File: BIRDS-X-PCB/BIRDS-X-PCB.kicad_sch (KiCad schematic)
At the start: 18 parts, among them J101 LPC-50M2LG

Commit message: Major layout
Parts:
- removed H105, H106, H107, H108, H109, H110, H111, H112, H113, H114, H115, H116: MountingHole, BIRDS-X_Footprints_Lib:MountingHole_2mm, symbol Mechanical:MountingHole
- removed TP101: TestPoint, TestPoint:TestPoint_Pad_D1.5mm, symbol Connector:TestPoint
- added J102, J103, J104: RFShield_OnePiece, RF_Shielding:Laird_Technologies_97-2003_12.70x13.37mm, symbol Device:RFShield_OnePiece
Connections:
- net GND: now also J102.1 (Shield), J103.1 (Shield), J104.1 (Shield)
- no-connect marks 40 -> 41
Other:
- added sheet TempSensors (TempSensors.kicad_sch)
- sheet RadfetExperiment ports: added none; removed I2C_SCL, I2C_SDA
- note removed: "Radiation Shielding Mounting"

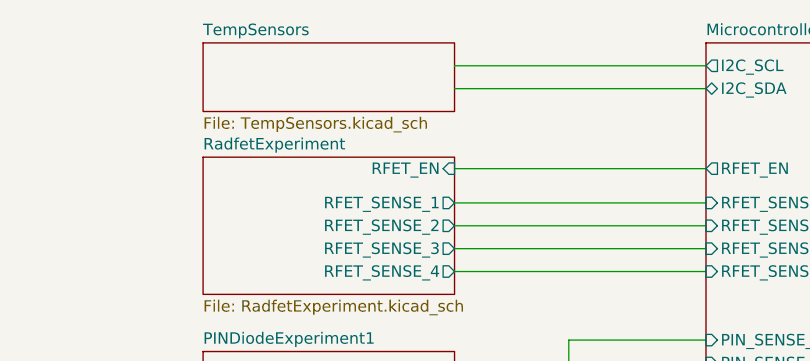
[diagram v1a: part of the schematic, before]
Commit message: Do most of routing
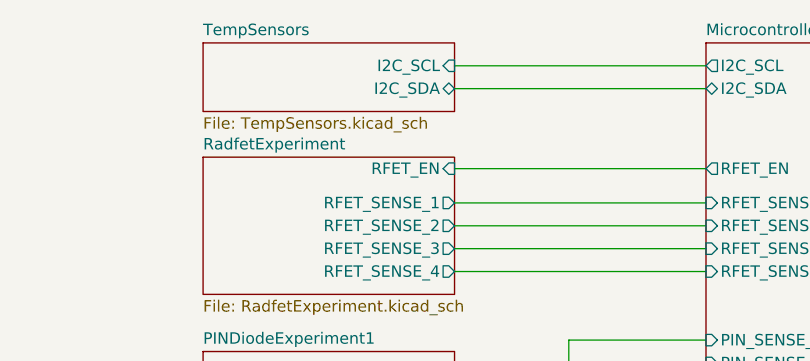
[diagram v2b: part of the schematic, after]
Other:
- sheet TempSensors ports: added I2C_SCL, I2C_SDA; removed none
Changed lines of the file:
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@@
       (effects (font (size 1.27 1.27)) (justify left top))
+    )
+    (pin "I2C_SCL" input (at 118.11 20.32 0)
+      (effects (font (size 1.27 1.27)) (justify right))
+    )
+    (pin "I2C_SDA" bidirectional (at 118.11 22.86 0)
+      (effects (font (size 1.27 1.27)) (justify right))
     )
     (instances

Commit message: Fix all DRC
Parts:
- J102, J103, J104: footprint RF_Shielding:Laird_Technologies_97-2003_12.70x13.37mm -> RF_Shielding:Laird_Technologies_BMI-S-101_13.66x12.70mm
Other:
- note added: "RF Shield Footprint: 12.70x13.66mm = 0.5 x 0.538""
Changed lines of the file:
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@@
     (stroke (width 0) (type default))
+  )
+  (text "RF Shield Footprint:\n12.70x13.66mm = 0.5 x 0.538\"" (at 58.42 134.62 0)
+    (effects (font (size 1.27 1.27)) (justify left bottom))
   )
   (text "Use SUP_3V3_2 as main power, per ICD" (at 195.58 118.11 0)
@@
       (effects (font (size 1.27 1.27)) (justify left))
     )
-    (property "Footprint" "RF_Shielding:Laird_Technologies_97-2003_12.70x13.37mm" (at 35.56 99.06 0)
+    (property "Footprint" "RF_Shielding:Laird_Technologies_BMI-S-101_13.66x12.70mm" (at 35.56 99.06 0)
       (effects (font (size 1.27 1.27)) hide)
     )
@@
       (effects (font (size 1.27 1.27)) (justify left))
     )
-    (property "Footprint" "RF_Shielding:Laird_Technologies_97-2003_12.70x13.37mm" (at 35.56 149.86 0)
+    (property "Footprint" "RF_Shielding:Laird_Technologies_BMI-S-101_13.66x12.70mm" (at 35.56 149.86 0)
       (effects (font (size 1.27 1.27)) hide)
     )
@@
       (effects (font (size 1.27 1.27)) (justify left))
     )
-    (property "Footprint" "RF_Shielding:Laird_Technologies_97-2003_12.70x13.37mm" (at 35.56 124.46 0)
-      (effects (font (size 1.27 1.27)) hide)
-    )
+    (property "Footprint" "RF_Shielding:Laird_Technologies_BMI-S-101_13.66x12.70mm" (at 35.56 124.46 0)
+      (effects (font (size 1.27 1.27)) hide)
+    )

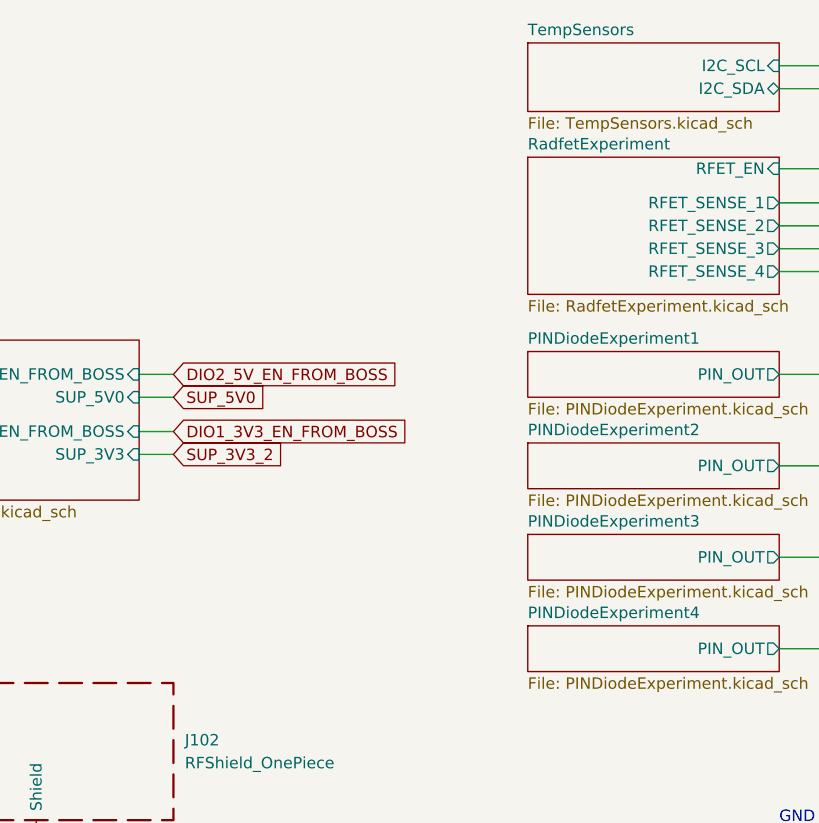
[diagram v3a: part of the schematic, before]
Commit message: Refactor jumper for PIN experiment power
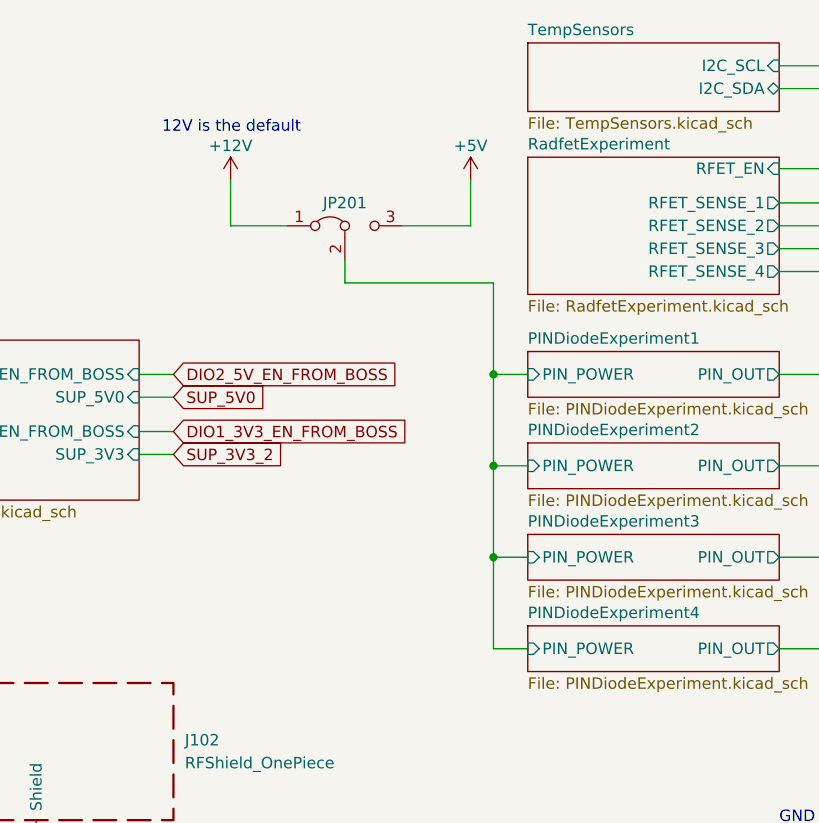
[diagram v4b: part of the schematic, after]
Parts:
- added JP201: Jumper_3_Bridged12, Jumper:SolderJumper-3_P1.3mm_Open_RoundedPad1.0x1.5mm_NumberLabels, symbol Jumper:Jumper_3_Bridged12
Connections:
- new net +12V: JP201.1 (A)
- new net +5V: JP201.3 (B)
- new net PINDiodeExperiment1/PIN_POWER: JP201.2 (C)
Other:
- sheet PINDiodeExperiment1 ports: added PIN_POWER; removed none
- sheet PINDiodeExperiment2 ports: added PIN_POWER; removed none
- sheet PINDiodeExperiment3 ports: added PIN_POWER; removed none
- sheet PINDiodeExperiment4 ports: added PIN_POWER; removed none
- note added: "12V is the default"
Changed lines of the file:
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@@
   (junction (at 181.61 102.87) (diameter 0) (color 0 0 0 0)
+  )
+  (junction (at 86.36 64.77) (diameter 0) (color 0 0 0 0)
+  )
+  (junction (at 86.36 54.61) (diameter 0) (color 0 0 0 0)
+  )
+  (junction (at 86.36 74.93) (diameter 0) (color 0 0 0 0)
   )
   (junction (at 181.61 105.41) (diameter 0) (color 0 0 0 0)
@@
     (stroke (width 0) (type default))
   )
+  (wire (pts (xy 90.17 64.77) (xy 86.36 64.77))
+    (stroke (width 0) (type default))
+  )
   (wire (pts (xy 187.96 41.91) (xy 205.74 41.91))
     (stroke (width 0) (type default))
@@
     (stroke (width 0) (type default))
   )
+  (wire (pts (xy 57.15 33.02) (xy 57.15 38.1))
+    (stroke (width 0) (type default))
+  )
   (wire (pts (xy 175.26 110.49) (xy 181.61 110.49))
     (stroke (width 0) (type default))
@@
     (stroke (width 0) (type default))
   )
+  (wire (pts (xy 86.36 44.45) (xy 86.36 54.61))
+    (stroke (width 0) (type default))
+  )
   (wire (pts (xy 181.61 101.6) (xy 181.61 102.87))
     (stroke (width 0) (type default))
@@
     (stroke (width 0) (type default))
   )
+  (wire (pts (xy 90.17 74.93) (xy 86.36 74.93))
+    (stroke (width 0) (type default))
+  )
+  (wire (pts (xy 69.85 44.45) (xy 86.36 44.45))
+    (stroke (width 0) (type default))
+  )
   (wire (pts (xy 181.61 105.41) (xy 194.31 105.41))
     (stroke (width 0) (type default))
@@
     (stroke (width 0) (type default))
   )
+  (wire (pts (xy 86.36 54.61) (xy 90.17 54.61))
+    (stroke (width 0) (type default))
+  )
   (wire (pts (xy 187.96 36.83) (xy 205.74 36.83))
     (stroke (width 0) (type default))
@@
     (stroke (width 0) (type default))
   )
+  (wire (pts (xy 83.82 33.02) (xy 83.82 38.1))
+    (stroke (width 0) (type default))
+  )
+  (wire (pts (xy 86.36 74.93) (xy 86.36 64.77))
+    (stroke (width 0) (type default))
+  )
   (wire (pts (xy 176.53 104.14) (xy 176.53 105.41))
     (stroke (width 0) (type default))
@@
     (stroke (width 0) (type default))
   )
+  (wire (pts (xy 90.17 85.09) (xy 86.36 85.09))
+    (stroke (width 0) (type default))
+  )
   (wire (pts (xy 118.11 85.09) (xy 138.43 85.09))
     (stroke (width 0) (type default))
@@
     (stroke (width 0) (type default))
   )
+  (wire (pts (xy 86.36 85.09) (xy 86.36 74.93))
+    (stroke (width 0) (type default))
+  )
   (wire (pts (xy 118.11 43.18) (xy 146.05 43.18))
     (stroke (width 0) (type default))
   )
+  (wire (pts (xy 86.36 64.77) (xy 86.36 54.61))
+    (stroke (width 0) (type default))
+  )
   (wire (pts (xy 135.89 74.93) (xy 135.89 55.88))
     (stroke (width 0) (type default))
@@
     (stroke (width 0) (type default))
   )
+  (wire (pts (xy 69.85 41.91) (xy 69.85 44.45))
+    (stroke (width 0) (type default))
+  )
   (wire (pts (xy 194.31 87.63) (xy 201.93 87.63))
     (stroke (width 0) (type default))
@@
     (stroke (width 0) (type default))
   )
+  (wire (pts (xy 57.15 38.1) (xy 63.5 38.1))
+    (stroke (width 0) (type default))
+  )
   (wire (pts (xy 142.24 101.6) (xy 142.24 105.41))
+    (stroke (width 0) (type default))
+  )
+  (wire (pts (xy 83.82 38.1) (xy 76.2 38.1))
     (stroke (width 0) (type default))
   )
@@
   (text "3-Pin Programming via Main Header:\n  1 - PROG_DBG_1 -> ST_SWDIO\n  2 - PROG_DBG_2 -> ST_SWDCLK\n  3 - PROG_DBG_3 -> ST_RST"
     (at 218.44 93.98 0)
+    (effects (font (size 1.27 1.27)) (justify left bottom))
+  )
+  (text "12V is the default" (at 49.53 27.94 0)
     (effects (font (size 1.27 1.27)) (justify left bottom))
   )
@@
     )
   )
+  (symbol (lib_id "Jumper:Jumper_3_Bridged12") (at 69.85 38.1 0) (unit 1)
+    (in_bom yes) (on_board yes) (dnp no)
+    (property "Reference" "JP201" (at 69.85 35.56 0)
+      (effects (font (size 1.27 1.27)))
+    )
+    (property "Value" "Jumper_3_Bridged12" (at 69.85 34.29 0)
+      (effects (font (size 1.27 1.27)) hide)
+    )
+    (property "Footprint" "Jumper:SolderJumper-3_P1.3mm_Open_RoundedPad1.0x1.5mm_NumberLabels" (at 69.85 38.1 0)
+      (effects (font (size 1.27 1.27)) hide)
+    )
+    (property "Datasheet" "~" (at 69.85 38.1 0)
+      (effects (font (size 1.27 1.27)) hide)
+    )
+    (pin "1")
+    (pin "2")
+    (pin "3")
+    (instances
+      (project "BIRDS-X-PCB"
+        (path "/c2796b15-795a-4d6e-ad4b-0ba87ded4bc9/f0b1214b-f453-423f-b2cf-f5d10e08eafe"
+          (reference "JP201") (unit 1)
+        )
+        (path "/c2796b15-795a-4d6e-ad4b-0ba87ded4bc9/69450ea3-1431-409d-8bc6-7752e7bc3ab3"
+          (reference "JP601") (unit 1)
+        )
+        (path "/c2796b15-795a-4d6e-ad4b-0ba87ded4bc9/24de0e99-26aa-4106-b99d-2d4b1437b640"
+          (reference "JP701") (unit 1)
+        )
+        (path "/c2796b15-795a-4d6e-ad4b-0ba87ded4bc9/20e9fdd9-b39a-4397-9a05-a4dbf181acd2"
+          (reference "JP801") (unit 1)
+        )
+        (path "/c2796b15-795a-4d6e-ad4b-0ba87ded4bc9/004149c1-7266-4be8-8957-13aaab4479fd"
+          (reference "JP901") (unit 1)
+        )
+        (path "/c2796b15-795a-4d6e-ad4b-0ba87ded4bc9"
+          (reference "JP101") (unit 1)
+        )
+      )
+    )
+  )
   (symbol (lib_id "Device:RFShield_OnePiece") (at 35.56 96.52 0) (unit 1)
     (in_bom yes) (on_board yes) (dnp no) (fields_autoplaced)
@@
     )
   )
+  (symbol (lib_id "power:+5V") (at 83.82 33.02 0) (unit 1)
+    (in_bom yes) (on_board yes) (dnp no) (fields_autoplaced)
+    (property "Reference" "#PWR0206" (at 83.82 36.83 0)
+      (effects (font (size 1.27 1.27)) hide)
+    )
+    (property "Value" "+5V" (at 83.82 29.21 0)
+      (effects (font (size 1.27 1.27)))
+    )
+    (property "Footprint" "" (at 83.82 33.02 0)
+      (effects (font (size 1.27 1.27)) hide)
+    )
+    (property "Datasheet" "" (at 83.82 33.02 0)
+      (effects (font (size 1.27 1.27)) hide)
+    )
+    (pin "1")
+    (instances
+      (project "BIRDS-X-PCB"
+        (path "/c2796b15-795a-4d6e-ad4b-0ba87ded4bc9/f0b1214b-f453-423f-b2cf-f5d10e08eafe"
+          (reference "#PWR0206") (unit 1)
+        )
+        (path "/c2796b15-795a-4d6e-ad4b-0ba87ded4bc9/69450ea3-1431-409d-8bc6-7752e7bc3ab3"
+          (reference "#PWR0602") (unit 1)
+        )
+        (path "/c2796b15-795a-4d6e-ad4b-0ba87ded4bc9/24de0e99-26aa-4106-b99d-2d4b1437b640"
+          (reference "#PWR0705") (unit 1)
+        )
+        (path "/c2796b15-795a-4d6e-ad4b-0ba87ded4bc9/20e9fdd9-b39a-4397-9a05-a4dbf181acd2"
+          (reference "#PWR0805") (unit 1)
+        )
+        (path "/c2796b15-795a-4d6e-ad4b-0ba87ded4bc9/004149c1-7266-4be8-8957-13aaab4479fd"
+          (reference "#PWR0905") (unit 1)
+        )
+        (path "/c2796b15-795a-4d6e-ad4b-0ba87ded4bc9"
+          (reference "#PWR0106") (unit 1)
+        )
+      )
+    )
+  )
   (symbol (lib_id "power:GND") (at 35.56 134.62 0) (unit 1)
     (in_bom yes) (on_board yes) (dnp no)
@@
         (path "/c2796b15-795a-4d6e-ad4b-0ba87ded4bc9"
           (reference "#PWR0103") (unit 1)
+        )
+      )
+    )
+  )
+  (symbol (lib_id "power:+12V") (at 57.15 33.02 0) (unit 1)
+    (in_bom yes) (on_board yes) (dnp no)
+    (property "Reference" "#PWR0607" (at 57.15 36.83 0)
+      (effects (font (size 1.27 1.27)) hide)
+    )
+    (property "Value" "+12V" (at 57.15 29.21 0)
+      (effects (font (size 1.27 1.27)))
+    )
+    (property "Footprint" "" (at 57.15 33.02 0)
+      (effects (font (size 1.27 1.27)) hide)
+    )
+    (property "Datasheet" "" (at 57.15 33.02 0)
+      (effects (font (size 1.27 1.27)) hide)
+    )
+    (pin "1")
+    (instances
+      (project "BIRDS-X-PCB"
+        (path "/c2796b15-795a-4d6e-ad4b-0ba87ded4bc9/69450ea3-1431-409d-8bc6-7752e7bc3ab3"
+          (reference "#PWR0607") (unit 1)
+        )
+        (path "/c2796b15-795a-4d6e-ad4b-0ba87ded4bc9/24de0e99-26aa-4106-b99d-2d4b1437b640"
+          (reference "#PWR0704") (unit 1)
+        )
+        (path "/c2796b15-795a-4d6e-ad4b-0ba87ded4bc9/20e9fdd9-b39a-4397-9a05-a4dbf181acd2"
+          (reference "#PWR0804") (unit 1)
+        )
+        (path "/c2796b15-795a-4d6e-ad4b-0ba87ded4bc9/004149c1-7266-4be8-8957-13aaab4479fd"
+          (reference "#PWR0904") (unit 1)
+        )
+        (path "/c2796b15-795a-4d6e-ad4b-0ba87ded4bc9"
+          (reference "#PWR0105") (unit 1)
         )
       )
@@
       (effects (font (size 1.27 1.27)) (justify right))
     )
+    (pin "PIN_POWER" input (at 90.17 85.09 180)
+      (effects (font (size 1.27 1.27)) (justify left))
+    )
     (instances
       (project "BIRDS-X-PCB"
@@
       (effects (font (size 1.27 1.27)) (justify right))
     )
+    (pin "PIN_POWER" input (at 90.17 74.93 180)
+      (effects (font (size 1.27 1.27)) (justify left))
+    )
     (instances
       (project "BIRDS-X-PCB"
@@
       (effects (font (size 1.27 1.27)) (justify right))
     )
+    (pin "PIN_POWER" input (at 90.17 64.77 180)
+      (effects (font (size 1.27 1.27)) (justify left))
+    )
     (instances
       (project "BIRDS-X-PCB"
@@
       (effects (font (size 1.27 1.27)) (justify right))
     )
-    (instances
+    (pin "PIN_POWER" input (at 90.17 54.61 180)
+      (effects (font (size 1.27 1.27)) (justify left))
+    )
+    (instances

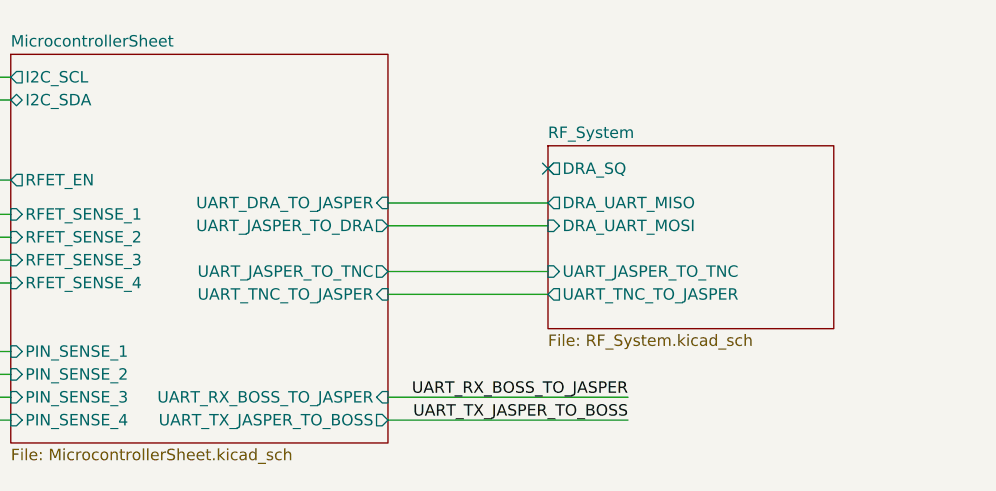
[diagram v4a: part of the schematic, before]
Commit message: Update to new STM32F103 MCU
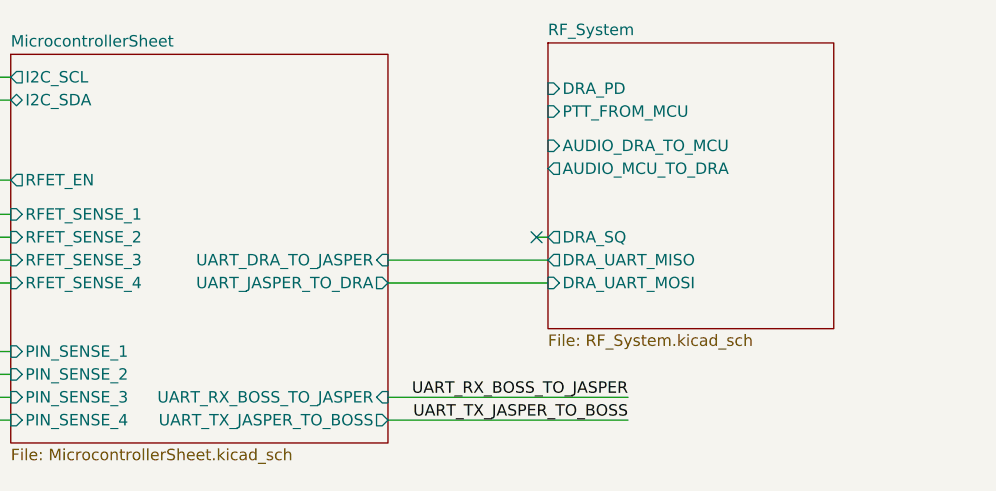
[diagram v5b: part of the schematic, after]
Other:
- sheet MicrocontrollerSheet ports: added none; removed UART_JASPER_TO_TNC, UART_TNC_TO_JASPER
- sheet RF_System ports: added AUDIO_DRA_TO_MCU, AUDIO_MCU_TO_DRA, DRA_PD, PTT_FROM_MCU; removed UART_JASPER_TO_TNC, UART_TNC_TO_JASPER
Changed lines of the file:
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@@
   (no_connect (at 194.31 143.51))
   (no_connect (at 181.61 115.57))
-  (no_connect (at 205.74 30.48))
+  (no_connect (at 204.47 38.1))
   (wire (pts (xy 187.96 55.88) (xy 214.63 55.88))
     (stroke (width 0) (type default))
@@
     (stroke (width 0) (type default))
   )
-  (wire (pts (xy 187.96 41.91) (xy 205.74 41.91))
-    (stroke (width 0) (type default))
-  )
   (wire (pts (xy 138.43 58.42) (xy 146.05 58.42))
     (stroke (width 0) (type default))
@@
     (stroke (width 0) (type default))
   )
-  (wire (pts (xy 187.96 36.83) (xy 205.74 36.83))
+  (wire (pts (xy 187.96 43.18) (xy 205.74 43.18))
     (stroke (width 0) (type default))
   )
@@
     (stroke (width 0) (type default))
   )
+  (wire (pts (xy 204.47 38.1) (xy 205.74 38.1))
+    (stroke (width 0) (type default))
+  )
   (wire (pts (xy 86.36 74.93) (xy 86.36 64.77))
     (stroke (width 0) (type default))
@@
     (stroke (width 0) (type default))
   )
-  (wire (pts (xy 187.96 34.29) (xy 205.74 34.29))
+  (wire (pts (xy 187.96 40.64) (xy 205.74 40.64))
     (stroke (width 0) (type default))
   )
@@
   )
   (wire (pts (xy 130.81 50.8) (xy 146.05 50.8))
-    (stroke (width 0) (type default))
-  )
-  (wire (pts (xy 187.96 44.45) (xy 205.74 44.45))
     (stroke (width 0) (type default))
   )
@@
     )
   )
-  (sheet (at 205.74 27.94) (size 31.75 20.32) (fields_autoplaced)
+  (sheet (at 205.74 16.51) (size 31.75 31.75) (fields_autoplaced)
     (stroke (width 0.1524) (type solid))
     (fill (color 0 0 0 0.0000))
-    (property "Sheetname" "RF_System" (at 205.74 27.2284 0)
+    (property "Sheetname" "RF_System" (at 205.74 15.7984 0)
       (effects (font (size 1.27 1.27)) (justify left bottom))
     )
@@
       (effects (font (size 1.27 1.27)) (justify left top))
     )
-    (pin "DRA_UART_MISO" output (at 205.74 34.29 180)
-      (effects (font (size 1.27 1.27)) (justify left))
-    )
-    (pin "DRA_UART_MOSI" input (at 205.74 36.83 180)
-      (effects (font (size 1.27 1.27)) (justify left))
-    )
-    (pin "DRA_SQ" output (at 205.74 30.48 180)
-      (effects (font (size 1.27 1.27)) (justify left))
-    )
-    (pin "UART_TNC_TO_JASPER" output (at 205.74 44.45 180)
-      (effects (font (size 1.27 1.27)) (justify left))
-    )
-    (pin "UART_JASPER_TO_TNC" input (at 205.74 41.91 180)
+    (pin "DRA_UART_MISO" output (at 205.74 40.64 180)
+      (effects (font (size 1.27 1.27)) (justify left))
+    )
+    (pin "DRA_UART_MOSI" input (at 205.74 43.18 180)
+      (effects (font (size 1.27 1.27)) (justify left))
+    )
+    (pin "DRA_SQ" output (at 205.74 38.1 180)
+      (effects (font (size 1.27 1.27)) (justify left))
+    )
+    (pin "DRA_PD" input (at 205.74 21.59 180)
+      (effects (font (size 1.27 1.27)) (justify left))
+    )
+    (pin "PTT_FROM_MCU" input (at 205.74 24.13 180)
+      (effects (font (size 1.27 1.27)) (justify left))
+    )
+    (pin "AUDIO_DRA_TO_MCU" input (at 205.74 27.94 180)
+      (effects (font (size 1.27 1.27)) (justify left))
+    )
+    (pin "AUDIO_MCU_TO_DRA" output (at 205.74 30.48 180)
       (effects (font (size 1.27 1.27)) (justify left))
     )
@@
       (effects (font (size 1.27 1.27)) (justify right))
     )
-    (pin "UART_JASPER_TO_TNC" output (at 187.96 41.91 0)
-      (effects (font (size 1.27 1.27)) (justify right))
-    )
-    (pin "UART_TNC_TO_JASPER" input (at 187.96 44.45 0)
-      (effects (font (size 1.27 1.27)) (justify right))
-    )
-    (pin "UART_JASPER_TO_DRA" output (at 187.96 36.83 0)
-      (effects (font (size 1.27 1.27)) (justify right))
-    )
-    (pin "UART_DRA_TO_JASPER" input (at 187.96 34.29 0)
-      (effects (font (size 1.27 1.27)) (justify right))
-    )
+    (pin "UART_JASPER_TO_DRA" output (at 187.96 43.18 0)
+      (effects (font (size 1.27 1.27)) (justify right))
+    )
+    (pin "UART_DRA_TO_JASPER" input (at 187.96 40.64 0)
+      (effects (font (size 1.27 1.27)) (justify right))
+    )
